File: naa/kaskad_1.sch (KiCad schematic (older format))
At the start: 16 parts, among them X1 Контрольная_точка_сопряжения, X2 Контрольная_точка_сопряжения

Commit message: готова схема, добавлены gerber и pdf
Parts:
- removed R5: Резистор_470_Ом±5%_0,1Вт, MOTOR_RLC:Резистор_SMD_0603-0,075_Вт, symbol MOTOR_2020_import:Резистор_470_Ом±5%_0,1Вт
- added RP2: Резистор_подстроечный_PVA3A102, MOTOR_IMPORT_OTK:резистор_подстроечный_PVZ3A334, symbol MOTOR_2020_import:Резистор_подстроечный_PVA3A102
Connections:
- net GND: now also RP2.2
- net at C2.2, X1.1: now also RP2.1
- no-connect marks 2 -> 3
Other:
- note added: "470 Ом"
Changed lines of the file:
@@
 $Descr A4 11693 8268
 encoding utf-8
-Sheet 2 2
+Sheet 3 3
 Title ""
 Date ""
@@
 AR Path="/5ECB1AF5" Ref="L?"  Part="1"
 AR Path="/5ECAE991/5ECB1AF5" Ref="L3"  Part="1"
-F 0 "L3" H 3750 2650 60  0000 C CNN
+AR Path="/5ED075B7/5ECB1AF5" Ref="L5"  Part="1"
+F 0 "L5" H 3750 2650 60  0000 C CNN
 F 1 "Чип-индуктивность_2,2_мкГн±10%" H 3650 2950 60  0001 C CNN
 F 2 "N_RLC:Чип-индуктивность_SMD_0805" H 3525 3075 60  0001 C CNN
@@
 AR Path="/5ECB1AFE" Ref="C?"  Part="1"
 AR Path="/5ECAE991/5ECB1AFE" Ref="C3"  Part="1"
-F 0 "C3" H 4400 2650 60  0000 C CNN
+AR Path="/5ED075B7/5ECB1AFE" Ref="C6"  Part="1"
+F 0 "C6" H 4400 2650 60  0000 C CNN
 F 1 "Конденсатор_подстроечный_TZC3R100A110" H 4350 2150 60  0001 C CNN
 F 2 "N_RLC:Конденсатор_подстроечный_TZC3" H 4250 2250 60  0001 C CNN
@@
 U 1 1 5ECB1CD0
 P 1600 2100
-F 0 "RP1" V 1950 1788 39  0000 L CNN
+AR Path="/5ECAE991/5ECB1CD0" Ref="RP1"  Part="1"
+AR Path="/5ED075B7/5ECB1CD0" Ref="RP3"  Part="1"
+F 0 "RP3" V 1950 1788 39  0000 L CNN
 F 1 "Резистор_подстроечный_PVZ3A105" H 2200 1200 39  0001 C CNN
 F 2 "MOTOR_IMPORT_OTK:резистор_подстроечный_PVZ3A334" H 2150 1100 39  0001 C CNN
@@
 U 1 1 5ECB362B
 P 2500 1650
-F 0 "R3" V 2750 1800 60  0000 C CNN
+AR Path="/5ECAE991/5ECB362B" Ref="R3"  Part="1"
+AR Path="/5ED075B7/5ECB362B" Ref="R7"  Part="1"
+F 0 "R7" V 2750 1800 60  0000 C CNN
 F 1 "Резистор_10_кОм±5%_0,1Вт" H 2825 1425 60  0001 C CNN
 F 2 "MOTOR_RLC:Резистор_SMD_0603-0,075_Вт" H 2350 1325 60  0001 C CNN
@@
 $EndComp
 $Comp
-L MOTOR_2020_import:Резистор_470_Ом±5%_0,1Вт R5
-U 1 1 5ECB78EF
-P 3250 5000
-F 0 "R5" V 3500 5150 60  0000 C CNN
-F 1 "Резистор_470_Ом±5%_0,1Вт" H 3575 4775 60  0001 C CNN
-F 2 "MOTOR_RLC:Резистор_SMD_0603-0,075_Вт" H 3100 4675 60  0001 C CNN
-F 3 "${MOTOR_2020_LIB}\\documentation\\Р1-12_СП.pdf" H 3550 5000 60  0001 C CNN
-F 4 "470 кОм" V 3600 5250 50  0000 C CNN "INFO"
-F 5 "https://www.chipdip.ru/product0/56821" H 3500 5250 50  0001 C CNN "LINK"
-	1    3250 5000
-	0    1    1    0
-$EndComp
-$Comp
 L MOTOR_2020_import:Резистор_1_кОм±5%_0,1Вт R2
 U 1 1 5ECB8169
 P 1400 3000
-F 0 "R2" H 1700 3150 60  0000 C CNN
+AR Path="/5ECAE991/5ECB8169" Ref="R2"  Part="1"
+AR Path="/5ED075B7/5ECB8169" Ref="R5"  Part="1"
+F 0 "R5" H 1700 3150 60  0000 C CNN
 F 1 "Резистор_1_кОм±5%_0,1Вт" H 1725 2775 60  0001 C CNN
 F 2 "MOTOR_RLC:Резистор_SMD_0603-0,075_Вт" H 1250 2675 60  0001 C CNN
@@
 U 1 1 5ECAF6A5
 P 2150 3000
-F 0 "VT1" H 2658 3098 60  0000 L CNN
+AR Path="/5ECAE991/5ECAF6A5" Ref="VT1"  Part="1"
+AR Path="/5ED075B7/5ECAF6A5" Ref="VT2"  Part="1"
+F 0 "VT2" H 2658 3098 60  0000 L CNN
 F 1 "Транзистор_КТ368Б9" H 2658 2992 60  0000 L CNN
 F 2 "MOTOR_VD_VT_HL:Корпус_КТ-46" H 2475 3625 60  0001 C CNN
@@
 U 1 1 5ECBB1CF
 P 2500 4000
-F 0 "R4" V 2750 4150 60  0000 C CNN
+AR Path="/5ECAE991/5ECBB1CF" Ref="R4"  Part="1"
+AR Path="/5ED075B7/5ECBB1CF" Ref="R8"  Part="1"
+F 0 "R8" V 2750 4150 60  0000 C CNN
 F 1 "Резистор_10_кОм±5%_0,1Вт" H 2825 3775 60  0001 C CNN
 F 2 "MOTOR_RLC:Резистор_SMD_0603-0,075_Вт" H 2350 3675 60  0001 C CNN
@@
 AR Path="/5ECBD277" Ref="C?"  Part="1"
 AR Path="/5ECAE991/5ECBD277" Ref="C2"  Part="1"
-F 0 "C2" V 3200 4750 60  0000 C CNN
+AR Path="/5ED075B7/5ECBD277" Ref="C5"  Part="1"
+F 0 "C5" V 3200 4750 60  0000 C CNN
 F 1 "Конденсатор_подстроечный_TZC3R100A110" H 3250 4250 60  0001 C CNN
 F 2 "N_RLC:Конденсатор_подстроечный_TZC3" H 3150 4350 60  0001 C CNN
@@
 AR Path="/5ECBD26A" Ref="L?"  Part="1"
 AR Path="/5ECAE991/5ECBD26A" Ref="L2"  Part="1"
-F 0 "L2" V 3000 4350 60  0000 C CNN
+AR Path="/5ED075B7/5ECBD26A" Ref="L4"  Part="1"
+F 0 "L4" V 3000 4350 60  0000 C CNN
 F 1 "Чип-индуктивность_2,2_мкГн±10%" H 2950 4650 60  0001 C CNN
 F 2 "N_RLC:Чип-индуктивность_SMD_0805" H 2825 4775 60  0001 C CNN
@@
 Wire Wire Line
 	2500 3500 2500 4000
-Wire Wire Line
-	2500 5750 3250 5750
-Wire Wire Line
-	3250 5750 3250 5600
 Connection ~ 2500 5750
 Wire Wire Line
@@
 U 1 1 5ECC9253
 P 4000 3400
-F 0 "XP3" H 4200 3450 50  0000 R CNN
+AR Path="/5ECAE991/5ECC9253" Ref="XP3"  Part="1"
+AR Path="/5ED075B7/5ECC9253" Ref="XP6"  Part="1"
+F 0 "XP6" H 4200 3450 50  0000 R CNN
 F 1 "Вилка_PLS-2" H 4150 2750 39  0001 C CNN
 F 2 "N_X:Вилка_PLS2_вертикальная" H 4250 2875 39  0001 C CNN
@@
 U 1 1 5ECCAC22
 P 3850 4900
-F 0 "X1" H 3850 5033 50  0000 C CNN
+AR Path="/5ECAE991/5ECCAC22" Ref="X1"  Part="1"
+AR Path="/5ED075B7/5ECCAC22" Ref="X3"  Part="1"
+F 0 "X3" H 3850 5033 50  0000 C CNN
 F 1 "Контрольная_точка_сопряжения" H 3725 5100 50  0001 C CNN
 F 2 "MOTOR_X:Пробник" H 3875 4700 50  0001 C CNN
@@
 U 1 1 5ECCF15F
 P 4000 1650
-F 0 "XP2" H 4200 1700 50  0000 R CNN
+AR Path="/5ECAE991/5ECCF15F" Ref="XP2"  Part="1"
+AR Path="/5ED075B7/5ECCF15F" Ref="XP5"  Part="1"
+F 0 "XP5" H 4200 1700 50  0000 R CNN
 F 1 "Вилка_PLS-2" H 4150 1000 39  0001 C CNN
 F 2 "N_X:Вилка_PLS2_вертикальная" H 4250 1125 39  0001 C CNN
@@
 U 1 1 5ECD2F56
 P 5500 2300
-F 0 "XP4" H 5700 2350 50  0000 R CNN
+AR Path="/5ECAE991/5ECD2F56" Ref="XP4"  Part="1"
+AR Path="/5ED075B7/5ECD2F56" Ref="XP7"  Part="1"
+F 0 "XP7" H 5700 2350 50  0000 R CNN
 F 1 "Вилка_PLS-3" H 5650 1650 39  0001 C CNN
 F 2 "N_X:Вилка_PLS3_вертикальная" H 5750 1775 39  0001 C CNN
@@
 U 1 1 5ECD58E9
 P 4750 4000
-F 0 "R6" V 5000 4150 60  0000 C CNN
+AR Path="/5ECAE991/5ECD58E9" Ref="R6"  Part="1"
+AR Path="/5ED075B7/5ECD58E9" Ref="R9"  Part="1"
+F 0 "R9" V 5000 4150 60  0000 C CNN
 F 1 "Резистор_470_Ом±5%_0,1Вт" H 5075 3775 60  0001 C CNN
 F 2 "MOTOR_RLC:Резистор_SMD_0603-0,075_Вт" H 4600 3675 60  0001 C CNN
@@
 	4750 2600 4750 3500
 Wire Wire Line
-	3250 5750 4750 5750
-Wire Wire Line
 	4750 5750 4750 4600
-Connection ~ 3250 5750
 Wire Wire Line
 	5000 2400 4750 2400
@@
 U 1 1 5ECDB0DC
 P 5350 3500
-F 0 "X2" H 5350 3633 50  0000 C CNN
+AR Path="/5ECAE991/5ECDB0DC" Ref="X2"  Part="1"
+AR Path="/5ED075B7/5ECDB0DC" Ref="X4"  Part="1"
+F 0 "X4" H 5350 3633 50  0000 C CNN
 F 1 "Контрольная_точка_сопряжения" H 5225 3700 50  0001 C CNN
 F 2 "MOTOR_X:Пробник" H 5375 3300 50  0001 C CNN
@@
 Text Label 2650 2500 0    50   ~ 0
 AMP_1
+$Comp
+L MOTOR_2020_import:Резистор_подстроечный_PVA3A102 RP2
+U 1 1 5ECF3568
+P 3850 4950
+AR Path="/5ECAE991/5ECF3568" Ref="RP2"  Part="1"
+AR Path="/5ED075B7/5ECF3568" Ref="RP4"  Part="1"
+F 0 "RP4" V 4050 4450 39  0000 L CNN
+F 1 "Резистор_подстроечный_PVA3A102" H 4450 4050 39  0001 C CNN
+F 2 "MOTOR_IMPORT_OTK:резистор_подстроечный_PVZ3A334" H 4400 3950 39  0001 C CNN
+F 3 "${MOTOR_2020_LIB}\\documentation\\IMPORT\\potentiometrs_PVZ.pdf" H 3850 4950 39  0001 C CNN
+F 4 "https://www.chipdip.ru/product/3303x-3-102" H 3850 4950 50  0001 C CNN "LINK"
+F 5 "1 кОм" H 3850 4950 50  0001 C CNN "INFO"
+	1    3850 4950
+	0    1    1    0
+$EndComp
+NoConn ~ 3250 5600
+Wire Wire Line
+	2500 5750 3450 5750
+Wire Wire Line
+	3450 5600 3450 5750
+Connection ~ 3450 5750
+Wire Wire Line
+	3450 5750 4750 5750
+Text Notes 3500 5400 0    50   ~ 0
+470 Ом
+Wire Notes Line
+	11400 1400 11400 5950
+Wire Notes Line
+	11400 5950 6400 5950
+Wire Notes Line
+	6400 5950 6400 1400
+Wire Notes Line
+	6400 1400 11400 1400
 $EndSCHEMATC

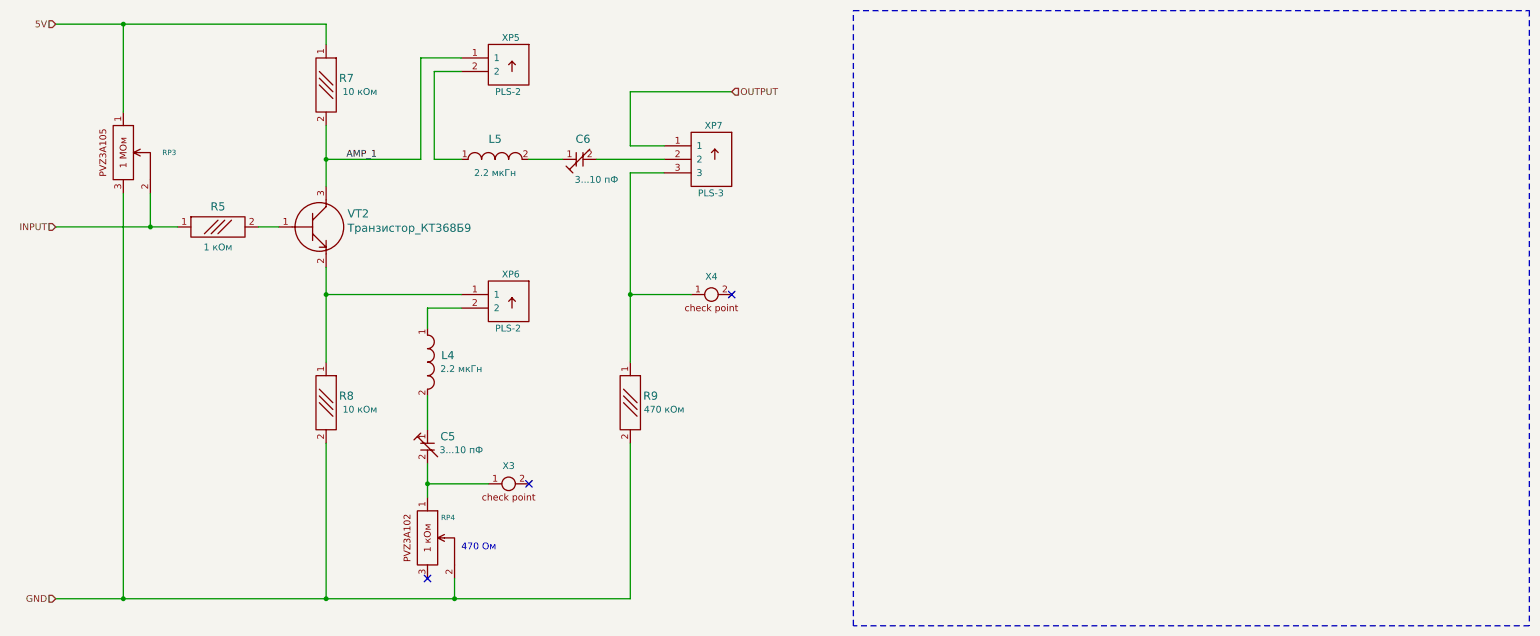
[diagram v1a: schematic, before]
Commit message: добавлены кондеи на питание, обновлены gerber и pdf
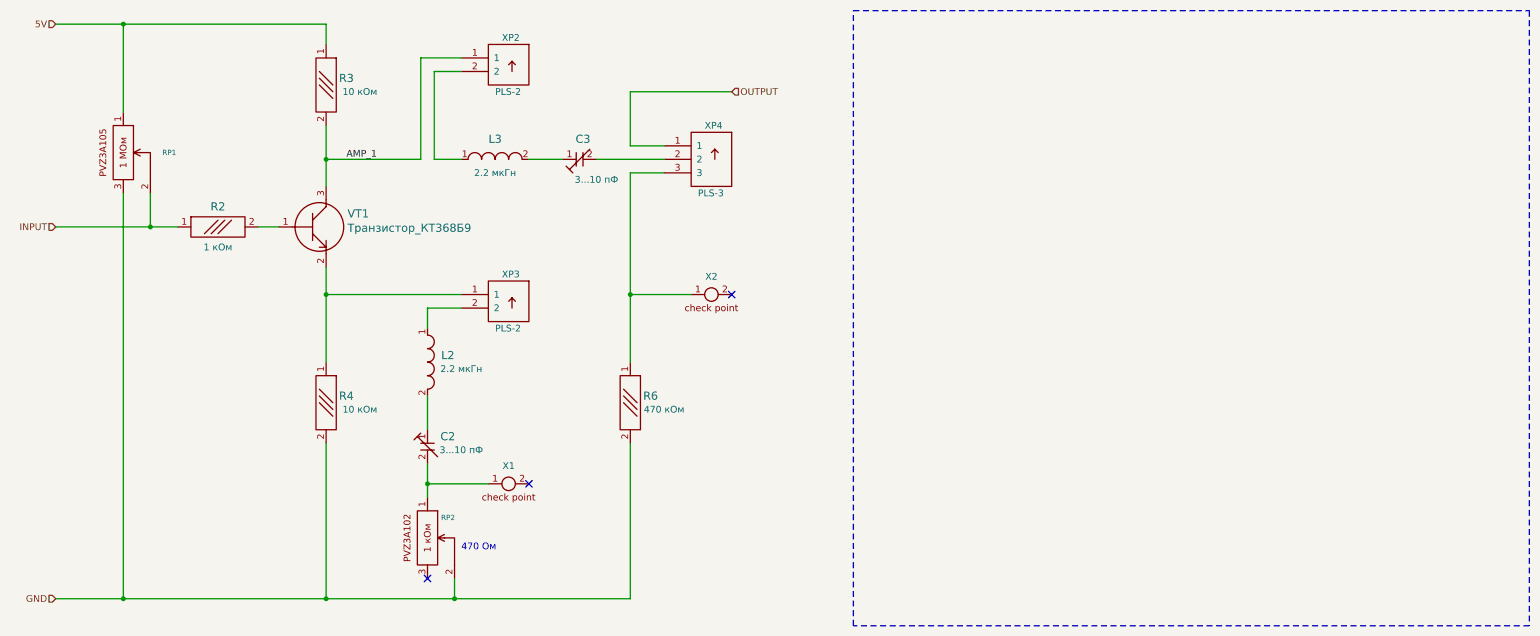
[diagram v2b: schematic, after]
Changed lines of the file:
@@
 $Descr A4 11693 8268
 encoding utf-8
-Sheet 3 3
+Sheet 2 3
 Title ""
 Date ""
@@
 AR Path="/5ECAE991/5ECB1AF5" Ref="L3"  Part="1"
 AR Path="/5ED075B7/5ECB1AF5" Ref="L5"  Part="1"
-F 0 "L5" H 3750 2650 60  0000 C CNN
+F 0 "L3" H 3750 2650 60  0000 C CNN
 F 1 "Чип-индуктивность_2,2_мкГн±10%" H 3650 2950 60  0001 C CNN
 F 2 "N_RLC:Чип-индуктивность_SMD_0805" H 3525 3075 60  0001 C CNN
@@
 AR Path="/5ECAE991/5ECB1AFE" Ref="C3"  Part="1"
 AR Path="/5ED075B7/5ECB1AFE" Ref="C6"  Part="1"
-F 0 "C6" H 4400 2650 60  0000 C CNN
+F 0 "C3" H 4400 2650 60  0000 C CNN
 F 1 "Конденсатор_подстроечный_TZC3R100A110" H 4350 2150 60  0001 C CNN
 F 2 "N_RLC:Конденсатор_подстроечный_TZC3" H 4250 2250 60  0001 C CNN
@@
 AR Path="/5ECAE991/5ECB1CD0" Ref="RP1"  Part="1"
 AR Path="/5ED075B7/5ECB1CD0" Ref="RP3"  Part="1"
-F 0 "RP3" V 1950 1788 39  0000 L CNN
+F 0 "RP1" V 1950 1788 39  0000 L CNN
 F 1 "Резистор_подстроечный_PVZ3A105" H 2200 1200 39  0001 C CNN
 F 2 "MOTOR_IMPORT_OTK:резистор_подстроечный_PVZ3A334" H 2150 1100 39  0001 C CNN
@@
 AR Path="/5ECAE991/5ECB362B" Ref="R3"  Part="1"
 AR Path="/5ED075B7/5ECB362B" Ref="R7"  Part="1"
-F 0 "R7" V 2750 1800 60  0000 C CNN
+F 0 "R3" V 2750 1800 60  0000 C CNN
 F 1 "Резистор_10_кОм±5%_0,1Вт" H 2825 1425 60  0001 C CNN
 F 2 "MOTOR_RLC:Резистор_SMD_0603-0,075_Вт" H 2350 1325 60  0001 C CNN
@@
 AR Path="/5ECAE991/5ECB8169" Ref="R2"  Part="1"
 AR Path="/5ED075B7/5ECB8169" Ref="R5"  Part="1"
-F 0 "R5" H 1700 3150 60  0000 C CNN
+F 0 "R2" H 1700 3150 60  0000 C CNN
 F 1 "Резистор_1_кОм±5%_0,1Вт" H 1725 2775 60  0001 C CNN
 F 2 "MOTOR_RLC:Резистор_SMD_0603-0,075_Вт" H 1250 2675 60  0001 C CNN
@@
 AR Path="/5ECAE991/5ECAF6A5" Ref="VT1"  Part="1"
 AR Path="/5ED075B7/5ECAF6A5" Ref="VT2"  Part="1"
-F 0 "VT2" H 2658 3098 60  0000 L CNN
+F 0 "VT1" H 2658 3098 60  0000 L CNN
 F 1 "Транзистор_КТ368Б9" H 2658 2992 60  0000 L CNN
 F 2 "MOTOR_VD_VT_HL:Корпус_КТ-46" H 2475 3625 60  0001 C CNN
@@
 AR Path="/5ECAE991/5ECBB1CF" Ref="R4"  Part="1"
 AR Path="/5ED075B7/5ECBB1CF" Ref="R8"  Part="1"
-F 0 "R8" V 2750 4150 60  0000 C CNN
+F 0 "R4" V 2750 4150 60  0000 C CNN
 F 1 "Резистор_10_кОм±5%_0,1Вт" H 2825 3775 60  0001 C CNN
 F 2 "MOTOR_RLC:Резистор_SMD_0603-0,075_Вт" H 2350 3675 60  0001 C CNN
@@
 AR Path="/5ECAE991/5ECBD277" Ref="C2"  Part="1"
 AR Path="/5ED075B7/5ECBD277" Ref="C5"  Part="1"
-F 0 "C5" V 3200 4750 60  0000 C CNN
+F 0 "C2" V 3200 4750 60  0000 C CNN
 F 1 "Конденсатор_подстроечный_TZC3R100A110" H 3250 4250 60  0001 C CNN
 F 2 "N_RLC:Конденсатор_подстроечный_TZC3" H 3150 4350 60  0001 C CNN
@@
 AR Path="/5ECAE991/5ECBD26A" Ref="L2"  Part="1"
 AR Path="/5ED075B7/5ECBD26A" Ref="L4"  Part="1"
-F 0 "L4" V 3000 4350 60  0000 C CNN
+F 0 "L2" V 3000 4350 60  0000 C CNN
 F 1 "Чип-индуктивность_2,2_мкГн±10%" H 2950 4650 60  0001 C CNN
 F 2 "N_RLC:Чип-индуктивность_SMD_0805" H 2825 4775 60  0001 C CNN
@@
 AR Path="/5ECAE991/5ECC9253" Ref="XP3"  Part="1"
 AR Path="/5ED075B7/5ECC9253" Ref="XP6"  Part="1"
-F 0 "XP6" H 4200 3450 50  0000 R CNN
+F 0 "XP3" H 4200 3450 50  0000 R CNN
 F 1 "Вилка_PLS-2" H 4150 2750 39  0001 C CNN
 F 2 "N_X:Вилка_PLS2_вертикальная" H 4250 2875 39  0001 C CNN
@@
 AR Path="/5ECAE991/5ECCAC22" Ref="X1"  Part="1"
 AR Path="/5ED075B7/5ECCAC22" Ref="X3"  Part="1"
-F 0 "X3" H 3850 5033 50  0000 C CNN
+F 0 "X1" H 3850 5033 50  0000 C CNN
 F 1 "Контрольная_точка_сопряжения" H 3725 5100 50  0001 C CNN
 F 2 "MOTOR_X:Пробник" H 3875 4700 50  0001 C CNN
@@
 AR Path="/5ECAE991/5ECCF15F" Ref="XP2"  Part="1"
 AR Path="/5ED075B7/5ECCF15F" Ref="XP5"  Part="1"
-F 0 "XP5" H 4200 1700 50  0000 R CNN
+F 0 "XP2" H 4200 1700 50  0000 R CNN
 F 1 "Вилка_PLS-2" H 4150 1000 39  0001 C CNN
 F 2 "N_X:Вилка_PLS2_вертикальная" H 4250 1125 39  0001 C CNN
@@
 AR Path="/5ECAE991/5ECD2F56" Ref="XP4"  Part="1"
 AR Path="/5ED075B7/5ECD2F56" Ref="XP7"  Part="1"
-F 0 "XP7" H 5700 2350 50  0000 R CNN
+F 0 "XP4" H 5700 2350 50  0000 R CNN
 F 1 "Вилка_PLS-3" H 5650 1650 39  0001 C CNN
 F 2 "N_X:Вилка_PLS3_вертикальная" H 5750 1775 39  0001 C CNN
@@
 AR Path="/5ECAE991/5ECD58E9" Ref="R6"  Part="1"
 AR Path="/5ED075B7/5ECD58E9" Ref="R9"  Part="1"
-F 0 "R9" V 5000 4150 60  0000 C CNN
+F 0 "R6" V 5000 4150 60  0000 C CNN
 F 1 "Резистор_470_Ом±5%_0,1Вт" H 5075 3775 60  0001 C CNN
 F 2 "MOTOR_RLC:Резистор_SMD_0603-0,075_Вт" H 4600 3675 60  0001 C CNN
@@
 AR Path="/5ECAE991/5ECDB0DC" Ref="X2"  Part="1"
 AR Path="/5ED075B7/5ECDB0DC" Ref="X4"  Part="1"
-F 0 "X4" H 5350 3633 50  0000 C CNN
+F 0 "X2" H 5350 3633 50  0000 C CNN
 F 1 "Контрольная_точка_сопряжения" H 5225 3700 50  0001 C CNN
 F 2 "MOTOR_X:Пробник" H 5375 3300 50  0001 C CNN
@@
 AR Path="/5ECAE991/5ECF3568" Ref="RP2"  Part="1"
 AR Path="/5ED075B7/5ECF3568" Ref="RP4"  Part="1"
-F 0 "RP4" V 4050 4450 39  0000 L CNN
+F 0 "RP2" V 4050 4450 39  0000 L CNN
 F 1 "Резистор_подстроечный_PVA3A102" H 4450 4050 39  0001 C CNN
 F 2 "MOTOR_IMPORT_OTK:резистор_подстроечный_PVZ3A334" H 4400 3950 39  0001 C CNN
